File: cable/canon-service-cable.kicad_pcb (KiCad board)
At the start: 2 copper layers, 12 x 33.4 mm, 3 parts, among them J1 Conn_02x04_Odd_Even, U1 service_connector

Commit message: Release: canon-service-cable v1.0
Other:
- board text added: "v1.0"
- board text removed: "Rev. 2"
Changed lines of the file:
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@@
       (effects (font (size 1.524 1.524) (thickness 0.3)) (justify mirror))
     )
-    (fp_poly (pts (xy -1.871133 0.6096) (xy -1.659467 0.6096) (xy -1.534165 0.606825) (xy -1.471682 0.589765)
-      (xy -1.450177 0.545316) (xy -1.4478 0.4826) (xy -1.4478 0.3556) (xy -2.167467 0.3556)
-      (xy -2.167467 1.6256) (xy -1.871133 1.6256) (xy -1.871133 0.6096)) (layer B.SilkS) (width 0.01))
-    (fp_poly (pts (xy -2.909821 1.350043) (xy -2.886659 1.208764) (xy -2.85749 1.123154) (xy -2.8292 1.100156)
-      (xy -2.808674 1.146712) (xy -2.802467 1.241807) (xy -2.793624 1.374776) (xy -2.776008 1.493308)
-      (xy -2.754386 1.57258) (xy -2.714453 1.611532) (xy -2.631104 1.62443) (xy -2.543175 1.6256)
-      (xy -2.3368 1.6256) (xy -2.3368 0.3556) (xy -2.5908 0.3556) (xy -2.5908 0.757766)
-      (xy -2.595023 0.947463) (xy -2.606777 1.083716) (xy -2.624696 1.153525) (xy -2.633133 1.159933)
-      (xy -2.667764 1.124554) (xy -2.675467 1.076996) (xy -2.681518 0.995918) (xy -2.697475 0.859116)
-      (xy -2.720044 0.694497) (xy -2.722946 0.674829) (xy -2.751374 0.507806) (xy -2.77921 0.409498)
-      (xy -2.812477 0.364212) (xy -2.845417 0.3556) (xy -2.895843 0.364125) (xy -2.93094 0.399907)
-      (xy -2.956314 0.478256) (xy -2.977575 0.614484) (xy -2.993895 0.760973) (xy -3.019233 0.961471)
-      (xy -3.043769 1.078453) (xy -3.065678 1.11179) (xy -3.083138 1.061351) (xy -3.094326 0.927008)
-      (xy -3.097513 0.76835) (xy -3.0988 0.3556) (xy -3.3528 0.3556) (xy -3.3528 1.6256)
-      (xy -2.93933 1.6256) (xy -2.909821 1.350043)) (layer B.SilkS) (width 0.01))
     (fp_poly (pts (xy -1.741838 2.754445) (xy -1.625447 2.721626) (xy -1.537565 2.660606) (xy -1.459613 2.56479)
       (xy -1.423442 2.509544) (xy -1.344963 2.404804) (xy -1.250776 2.32673) (xy -1.124916 2.268621)
@@
       (xy -2.330905 2.753629) (xy -2.136225 2.761787) (xy -2.134465 2.761847) (xy -1.905318 2.765654)
       (xy -1.741838 2.754445)) (layer B.SilkS) (width 0.01))
+    (fp_poly (pts (xy -2.909821 1.350043) (xy -2.886659 1.208764) (xy -2.85749 1.123154) (xy -2.8292 1.100156)
+      (xy -2.808674 1.146712) (xy -2.802467 1.241807) (xy -2.793624 1.374776) (xy -2.776008 1.493308)
+      (xy -2.754386 1.57258) (xy -2.714453 1.611532) (xy -2.631104 1.62443) (xy -2.543175 1.6256)
+      (xy -2.3368 1.6256) (xy -2.3368 0.3556) (xy -2.5908 0.3556) (xy -2.5908 0.757766)
+      (xy -2.595023 0.947463) (xy -2.606777 1.083716) (xy -2.624696 1.153525) (xy -2.633133 1.159933)
+      (xy -2.667764 1.124554) (xy -2.675467 1.076996) (xy -2.681518 0.995918) (xy -2.697475 0.859116)
+      (xy -2.720044 0.694497) (xy -2.722946 0.674829) (xy -2.751374 0.507806) (xy -2.77921 0.409498)
+      (xy -2.812477 0.364212) (xy -2.845417 0.3556) (xy -2.895843 0.364125) (xy -2.93094 0.399907)
+      (xy -2.956314 0.478256) (xy -2.977575 0.614484) (xy -2.993895 0.760973) (xy -3.019233 0.961471)
+      (xy -3.043769 1.078453) (xy -3.065678 1.11179) (xy -3.083138 1.061351) (xy -3.094326 0.927008)
+      (xy -3.097513 0.76835) (xy -3.0988 0.3556) (xy -3.3528 0.3556) (xy -3.3528 1.6256)
+      (xy -2.93933 1.6256) (xy -2.909821 1.350043)) (layer B.SilkS) (width 0.01))
+    (fp_poly (pts (xy -1.871133 0.6096) (xy -1.659467 0.6096) (xy -1.534165 0.606825) (xy -1.471682 0.589765)
+      (xy -1.450177 0.545316) (xy -1.4478 0.4826) (xy -1.4478 0.3556) (xy -2.167467 0.3556)
+      (xy -2.167467 1.6256) (xy -1.871133 1.6256) (xy -1.871133 0.6096)) (layer B.SilkS) (width 0.01))
   )
   (module Connector_IDC:IDC-Header_2x04_P2.54mm_Horizontal (layer F.Cu)
@@
       (effects (font (size 1 1) (thickness 0.15)))
     )
+    (fp_line (start 4.38 -4.1) (end 5.38 -5.1) (layer F.Fab) (width 0.1))
+    (fp_line (start 4.38 1.76) (end 13.28 1.76) (layer F.Fab) (width 0.1))
+    (fp_line (start 4.38 5.86) (end 13.28 5.86) (layer F.Fab) (width 0.1))
+    (fp_line (start 4.27 1.76) (end 13.39 1.76) (layer F.SilkS) (width 0.12))
+    (fp_line (start 4.27 5.86) (end 13.39 5.86) (layer F.SilkS) (width 0.12))
+    (fp_line (start 4.38 -0.32) (end -0.32 -0.32) (layer F.Fab) (width 0.1))
+    (fp_line (start -0.32 -0.32) (end -0.32 0.32) (layer F.Fab) (width 0.1))
+    (fp_line (start -0.32 0.32) (end 4.38 0.32) (layer F.Fab) (width 0.1))
+    (fp_line (start 4.38 2.22) (end -0.32 2.22) (layer F.Fab) (width 0.1))
+    (fp_line (start -0.32 2.22) (end -0.32 2.86) (layer F.Fab) (width 0.1))
+    (fp_line (start -0.32 2.86) (end 4.38 2.86) (layer F.Fab) (width 0.1))
+    (fp_line (start 4.38 4.76) (end -0.32 4.76) (layer F.Fab) (width 0.1))
+    (fp_line (start -0.32 4.76) (end -0.32 5.4) (layer F.Fab) (width 0.1))
+    (fp_line (start -0.32 5.4) (end 4.38 5.4) (layer F.Fab) (width 0.1))
+    (fp_line (start 4.38 7.3) (end -0.32 7.3) (layer F.Fab) (width 0.1))
+    (fp_line (start -0.32 7.3) (end -0.32 7.94) (layer F.Fab) (width 0.1))
+    (fp_line (start -0.32 7.94) (end 4.38 7.94) (layer F.Fab) (width 0.1))
+    (fp_line (start 5.38 -5.1) (end 13.28 -5.1) (layer F.Fab) (width 0.1))
+    (fp_line (start 13.28 -5.1) (end 13.28 12.72) (layer F.Fab) (width 0.1))
+    (fp_line (start 13.28 12.72) (end 4.38 12.72) (layer F.Fab) (width 0.1))
+    (fp_line (start 4.38 12.72) (end 4.38 -4.1) (layer F.Fab) (width 0.1))
+    (fp_line (start 4.27 -5.21) (end 13.39 -5.21) (layer F.SilkS) (width 0.12))
+    (fp_line (start 13.39 -5.21) (end 13.39 12.83) (layer F.SilkS) (width 0.12))
+    (fp_line (start 13.39 12.83) (end 4.27 12.83) (layer F.SilkS) (width 0.12))
+    (fp_line (start 4.27 12.83) (end 4.27 -5.21) (layer F.SilkS) (width 0.12))
+    (fp_line (start -1.35 0) (end -2.35 -0.5) (layer F.SilkS) (width 0.12))
+    (fp_line (start -2.35 -0.5) (end -2.35 0.5) (layer F.SilkS) (width 0.12))
+    (fp_line (start -2.35 0.5) (end -1.35 0) (layer F.SilkS) (width 0.12))
+    (fp_line (start -1.35 -5.6) (end -1.35 13.22) (layer F.CrtYd) (width 0.05))
+    (fp_line (start -1.35 13.22) (end 13.78 13.22) (layer F.CrtYd) (width 0.05))
+    (fp_line (start 13.78 13.22) (end 13.78 -5.6) (layer F.CrtYd) (width 0.05))
     (fp_line (start 13.78 -5.6) (end -1.35 -5.6) (layer F.CrtYd) (width 0.05))
-    (fp_line (start 13.78 13.22) (end 13.78 -5.6) (layer F.CrtYd) (width 0.05))
-    (fp_line (start -1.35 13.22) (end 13.78 13.22) (layer F.CrtYd) (width 0.05))
-    (fp_line (start -1.35 -5.6) (end -1.35 13.22) (layer F.CrtYd) (width 0.05))
-    (fp_line (start -2.35 0.5) (end -1.35 0) (layer F.SilkS) (width 0.12))
-    (fp_line (start -2.35 -0.5) (end -2.35 0.5) (layer F.SilkS) (width 0.12))
-    (fp_line (start -1.35 0) (end -2.35 -0.5) (layer F.SilkS) (width 0.12))
-    (fp_line (start 4.27 12.83) (end 4.27 -5.21) (layer F.SilkS) (width 0.12))
-    (fp_line (start 13.39 12.83) (end 4.27 12.83) (layer F.SilkS) (width 0.12))
-    (fp_line (start 13.39 -5.21) (end 13.39 12.83) (layer F.SilkS) (width 0.12))
-    (fp_line (start 4.27 -5.21) (end 13.39 -5.21) (layer F.SilkS) (width 0.12))
-    (fp_line (start 4.38 12.72) (end 4.38 -4.1) (layer F.Fab) (width 0.1))
-    (fp_line (start 13.28 12.72) (end 4.38 12.72) (layer F.Fab) (width 0.1))
-    (fp_line (start 13.28 -5.1) (end 13.28 12.72) (layer F.Fab) (width 0.1))
-    (fp_line (start 5.38 -5.1) (end 13.28 -5.1) (layer F.Fab) (width 0.1))
-    (fp_line (start -0.32 7.94) (end 4.38 7.94) (layer F.Fab) (width 0.1))
-    (fp_line (start -0.32 7.3) (end -0.32 7.94) (layer F.Fab) (width 0.1))
-    (fp_line (start 4.38 7.3) (end -0.32 7.3) (layer F.Fab) (width 0.1))
-    (fp_line (start -0.32 5.4) (end 4.38 5.4) (layer F.Fab) (width 0.1))
-    (fp_line (start -0.32 4.76) (end -0.32 5.4) (layer F.Fab) (width 0.1))
-    (fp_line (start 4.38 4.76) (end -0.32 4.76) (layer F.Fab) (width 0.1))
-    (fp_line (start -0.32 2.86) (end 4.38 2.86) (layer F.Fab) (width 0.1))
-    (fp_line (start -0.32 2.22) (end -0.32 2.86) (layer F.Fab) (width 0.1))
-    (fp_line (start 4.38 2.22) (end -0.32 2.22) (layer F.Fab) (width 0.1))
-    (fp_line (start -0.32 0.32) (end 4.38 0.32) (layer F.Fab) (width 0.1))
-    (fp_line (start -0.32 -0.32) (end -0.32 0.32) (layer F.Fab) (width 0.1))
-    (fp_line (start 4.38 -0.32) (end -0.32 -0.32) (layer F.Fab) (width 0.1))
-    (fp_line (start 4.27 5.86) (end 13.39 5.86) (layer F.SilkS) (width 0.12))
-    (fp_line (start 4.27 1.76) (end 13.39 1.76) (layer F.SilkS) (width 0.12))
-    (fp_line (start 4.38 5.86) (end 13.28 5.86) (layer F.Fab) (width 0.1))
-    (fp_line (start 4.38 1.76) (end 13.28 1.76) (layer F.Fab) (width 0.1))
-    (fp_line (start 4.38 -4.1) (end 5.38 -5.1) (layer F.Fab) (width 0.1))
     (fp_text user %R (at 8.83 3.81) (layer F.Fab)
       (effects (font (size 1 1) (thickness 0.15)))
@@
     )
   )
-  (gr_text "Rev. 2" (at 50.1 54.9) (layer B.SilkS)
-    (effects (font (size 0.5 0.5) (thickness 0.125)) (justify mirror))
+  (gr_text v1.0 (at 50.02784 55.04942) (layer B.SilkS)
+    (effects (font (size 0.75 0.75) (thickness 0.125)) (justify mirror))
   )
   (gr_text 10/2020 (at 49.9237 44.7929) (layer B.SilkS)

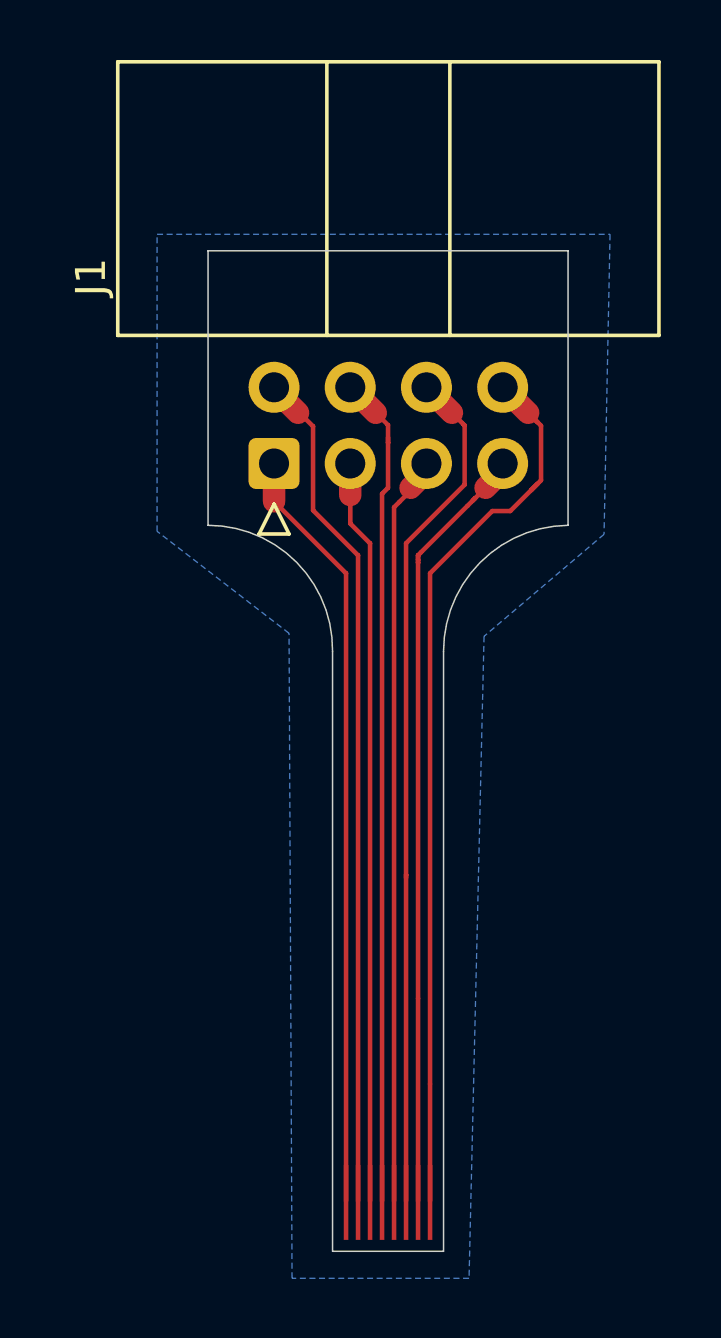
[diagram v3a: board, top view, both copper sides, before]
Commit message: cable: round up corners on connector
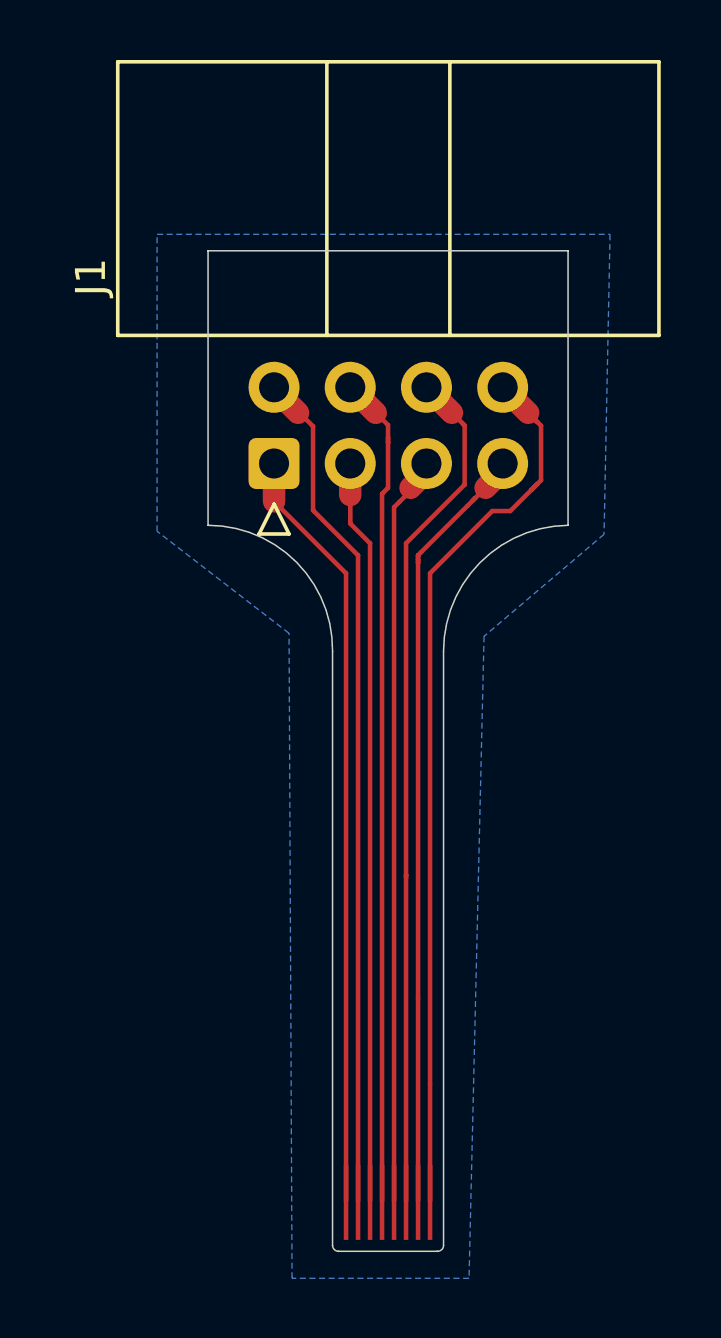
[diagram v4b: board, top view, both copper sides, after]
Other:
- outline, holes or cut-outs redrawn
- net class Default removed
- board text added: "03/2022"
- board text added: "v1.1"
- board text removed: "10/2020"
- board text removed: "v1.0"
